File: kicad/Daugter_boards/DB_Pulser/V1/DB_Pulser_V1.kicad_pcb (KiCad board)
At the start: 2 copper layers, 43.2 x 50.8 mm, 28 parts, among them P1 CONN_01X19, P2 CONN_01X02, P3 CONN_01X19, P4 CONN_01X02, P5 SMA, Q1 Q2N2222, Q2 Q2N2907, Q3 Q2N2222, Q4 Q2N2907, Q5 Q2N2222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

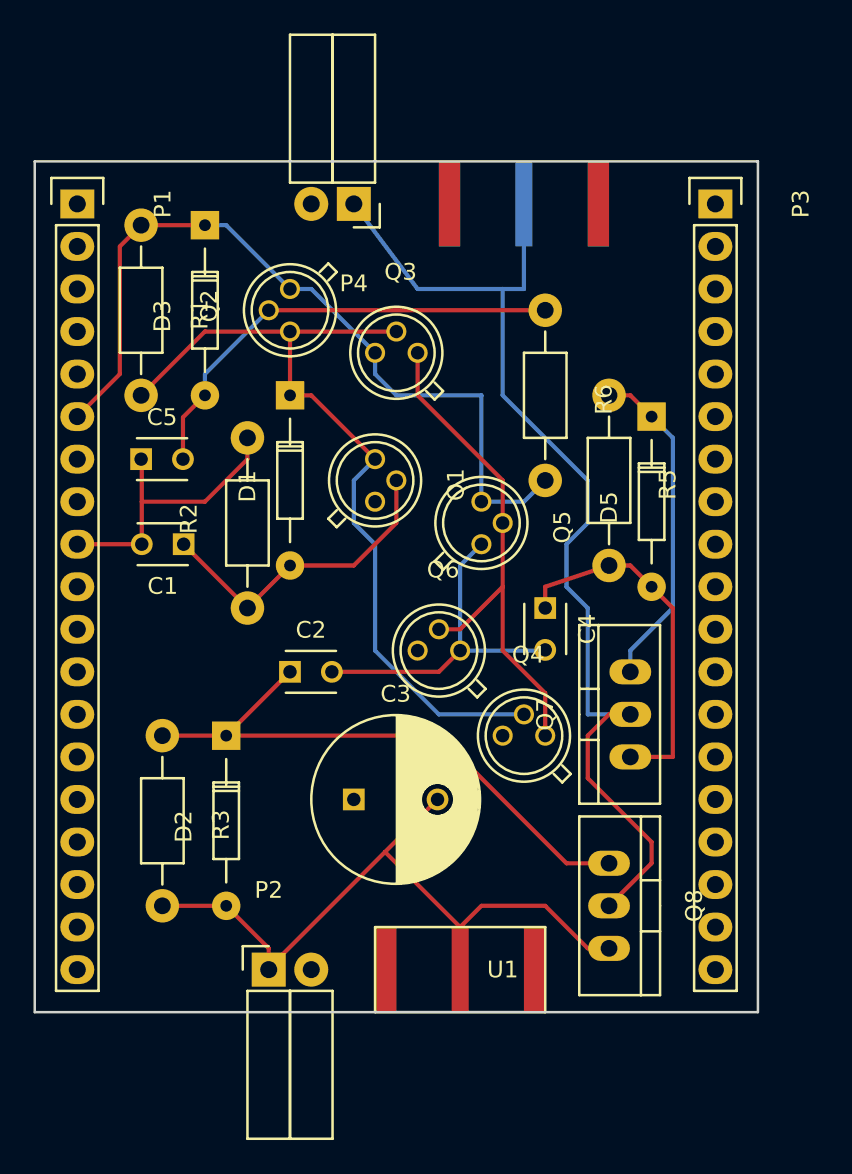
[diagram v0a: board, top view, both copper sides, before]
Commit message: update DB_HV, update librairy and librairy path for MDL
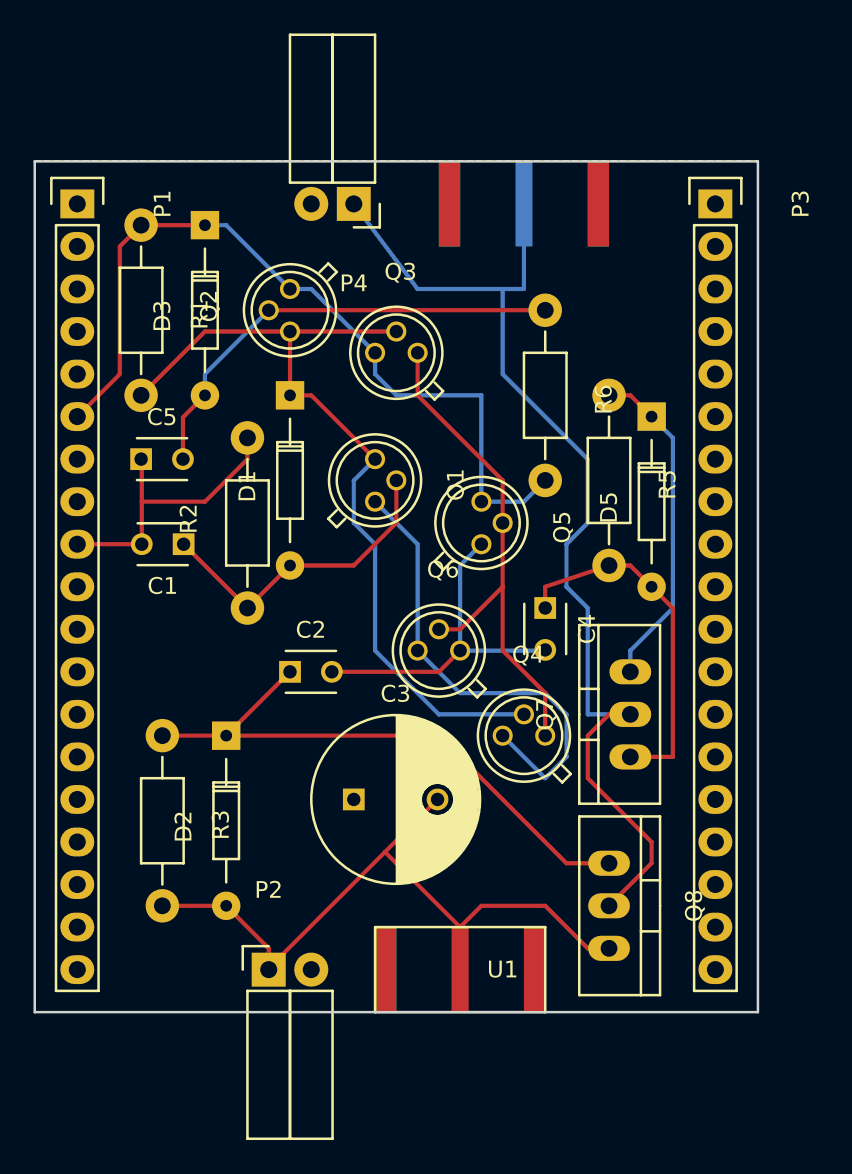
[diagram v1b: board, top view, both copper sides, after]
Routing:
- net GND: track 0.00 -> 28.3 mm
- added copper zone on B.Cu, net GND
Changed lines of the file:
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@@
   (general
     (links 57)
-    (no_connects 6)
-    (area 39.294999 78.664999 82.625001 129.615001)
+    (no_connects 0)
+    (area 39.294999 70.454999 86.185 137.825001)
     (thickness 1.6)
     (drawings 4)
-    (tracks 116)
+    (tracks 124)
     (zones 0)
     (modules 28)
@@
       (outputformat 1)
       (mirror false)
-      (drillshape 1)
+      (drillshape 0)
       (scaleselection 1)
-      (outputdirectory ""))
+      (outputdirectory gerber/))
   )
   (net 0 "")
@@
   (segment (start 57.11 109.22) (end 63.5 109.22) (width 0.25) (layer F.Cu) (net 4))
   (segment (start 63.5 109.22) (end 64.77 107.95) (width 0.25) (layer F.Cu) (net 4))
+  (segment (start 62.23 107.95) (end 62.23 101.6) (width 0.25) (layer B.Cu) (net 5))
+  (segment (start 62.23 101.6) (end 59.69 99.06) (width 0.25) (layer B.Cu) (net 5))
+  (segment (start 62.23 107.95) (end 64.77 110.49) (width 0.25) (layer B.Cu) (net 5))
+  (segment (start 69.85 115.57) (end 67.31 113.03) (width 0.25) (layer B.Cu) (net 5))
+  (segment (start 71.12 114.3) (end 69.85 115.57) (width 0.25) (layer B.Cu) (net 5))
+  (segment (start 71.12 111.76) (end 71.12 114.3) (width 0.25) (layer B.Cu) (net 5))
+  (segment (start 69.85 110.49) (end 71.12 111.76) (width 0.25) (layer B.Cu) (net 5))
+  (segment (start 64.77 110.49) (end 69.85 110.49) (width 0.25) (layer B.Cu) (net 5))
   (segment (start 73.66 125.73) (end 72.39 125.73) (width 0.25) (layer F.Cu) (net 6))
   (segment (start 66.04 123.19) (end 64.77 124.46) (width 0.25) (layer F.Cu) (net 6))
@@
   (segment (start 58.42 81.28) (end 62.23 86.36) (width 0.25) (layer B.Cu) (net 46) (status 10))
   (segment (start 62.23 86.36) (end 67.31 86.36) (width 0.25) (layer B.Cu) (net 46))
-  (segment (start 67.31 86.36) (end 67.31 92.71) (width 0.25) (layer B.Cu) (net 46))
+  (segment (start 67.31 86.36) (end 67.31 91.44) (width 0.25) (layer B.Cu) (net 46))
   (segment (start 72.39 111.76) (end 74.93 111.76) (width 0.25) (layer B.Cu) (net 46))
   (segment (start 72.39 105.41) (end 72.39 111.76) (width 0.25) (layer B.Cu) (net 46))
@@
   (segment (start 71.12 101.6) (end 71.12 104.14) (width 0.25) (layer B.Cu) (net 46))
   (segment (start 72.39 100.33) (end 71.12 101.6) (width 0.25) (layer B.Cu) (net 46))
-  (segment (start 72.39 97.79) (end 72.39 100.33) (width 0.25) (layer B.Cu) (net 46))
-  (segment (start 67.31 92.71) (end 72.39 97.79) (width 0.25) (layer B.Cu) (net 46))
+  (segment (start 72.39 96.52) (end 72.39 100.33) (width 0.25) (layer B.Cu) (net 46))
+  (segment (start 67.31 91.44) (end 72.39 96.52) (width 0.25) (layer B.Cu) (net 46))
   (segment (start 68.58 86.36) (end 68.58 81.28) (width 0.25) (layer B.Cu) (net 46) (status 20))
   (segment (start 67.31 86.36) (end 68.58 86.36) (width 0.25) (layer B.Cu) (net 46))
@@
     (connect_pads (clearance 0.508))
     (min_thickness 0.254)
+    (fill yes (arc_segments 16) (thermal_gap 0.508) (thermal_bridge_width 0.508))
+    (polygon
+      (pts
+        (xy 82.55 129.54) (xy 39.37 129.54) (xy 39.37 78.74) (xy 82.55 78.74)
+      )
+    )
+  )
+  (zone (net 5) (net_name GND) (layer B.Cu) (hatch edge 0.508)
+    (connect_pads (clearance 0.508))
+    (min_thickness 0.254)
